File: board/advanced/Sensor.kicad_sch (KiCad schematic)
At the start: 18 parts, among them U6 INA260, U7 BNO086, U8 BME280, Y2 ABS06-32.768KHZ-T

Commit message: put footprints and change schematics
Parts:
- R18: renamed from R20; footprint Resistor_SMD:R_0603_1608Metric -> Resistor_SMD:R_0402_1005Metric
- R19: renamed from R21; footprint Resistor_SMD:R_0603_1608Metric -> Resistor_SMD:R_0402_1005Metric
- R20: renamed from R22; footprint Resistor_SMD:R_0603_1608Metric -> Resistor_SMD:R_0402_1005Metric
- TP1: footprint TestPoint:TestPoint_Loop_D2.50mm_Drill1.85mm -> TestPoint:TestPoint_THTPad_2.0x2.0mm_Drill1.0mm
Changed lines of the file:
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@@
 		(on_board yes)
 		(dnp no)
-		(property "Reference" "#PWR057"
+		(property "Reference" "#PWR059"
 			(at 177.8 100.33 0)
 			(hide yes)
@@
 			(project "TurtlePico-Minimal"
 				(path "/7af2d99d-e350-48e7-86b4-20911ea922f3/399e14dd-2b99-438e-9945-456c74135ff2"
-					(reference "#PWR057")
+					(reference "#PWR059")
 					(unit 1)
 				)
@@
 		(on_board yes)
 		(dnp no)
-		(property "Reference" "#PWR048"
+		(property "Reference" "#PWR050"
 			(at 114.3 93.98 0)
 			(hide yes)
@@
 			(project "TurtlePico-Minimal"
 				(path "/7af2d99d-e350-48e7-86b4-20911ea922f3/399e14dd-2b99-438e-9945-456c74135ff2"
-					(reference "#PWR048")
+					(reference "#PWR050")
 					(unit 1)
 				)
@@
 		(on_board yes)
 		(dnp no)
-		(property "Reference" "#PWR052"
+		(property "Reference" "#PWR054"
 			(at 151.13 119.38 0)
 			(hide yes)
@@
 			(project "TurtlePico-Minimal"
 				(path "/7af2d99d-e350-48e7-86b4-20911ea922f3/399e14dd-2b99-438e-9945-456c74135ff2"
-					(reference "#PWR052")
+					(reference "#PWR054")
 					(unit 1)
 				)
@@
 		(on_board yes)
 		(dnp no)
-		(property "Reference" "#PWR049"
+		(property "Reference" "#PWR051"
 			(at 115.57 52.07 0)
 			(hide yes)
@@
 			(project "TurtlePico-Minimal"
 				(path "/7af2d99d-e350-48e7-86b4-20911ea922f3/399e14dd-2b99-438e-9945-456c74135ff2"
-					(reference "#PWR049")
+					(reference "#PWR051")
 					(unit 1)
 				)
@@
 		(on_board yes)
 		(dnp no)
-		(property "Reference" "#PWR056"
+		(property "Reference" "#PWR058"
 			(at 168.91 143.51 0)
 			(hide yes)
@@
 			(project "TurtlePico-Minimal"
 				(path "/7af2d99d-e350-48e7-86b4-20911ea922f3/399e14dd-2b99-438e-9945-456c74135ff2"
-					(reference "#PWR056")
+					(reference "#PWR058")
 					(unit 1)
 				)
@@
 		(on_board yes)
 		(dnp no)
-		(property "Reference" "#PWR042"
+		(property "Reference" "#PWR044"
 			(at 87.63 119.38 0)
 			(hide yes)
@@
 			(project "TurtlePico-Minimal"
 				(path "/7af2d99d-e350-48e7-86b4-20911ea922f3/399e14dd-2b99-438e-9945-456c74135ff2"
-					(reference "#PWR042")
+					(reference "#PWR044")
 					(unit 1)
 				)
@@
 		(on_board yes)
 		(dnp no)
-		(property "Reference" "#PWR044"
+		(property "Reference" "#PWR046"
 			(at 96.52 77.47 0)
 			(hide yes)
@@
 			(project "TurtlePico-Minimal"
 				(path "/7af2d99d-e350-48e7-86b4-20911ea922f3/399e14dd-2b99-438e-9945-456c74135ff2"
-					(reference "#PWR044")
+					(reference "#PWR046")
 					(unit 1)
 				)
@@
 		(on_board yes)
 		(dnp no)
-		(property "Reference" "#PWR051"
+		(property "Reference" "#PWR053"
 			(at 129.54 133.35 0)
 			(hide yes)
@@
 			(project "TurtlePico-Minimal"
 				(path "/7af2d99d-e350-48e7-86b4-20911ea922f3/399e14dd-2b99-438e-9945-456c74135ff2"
-					(reference "#PWR051")
+					(reference "#PWR053")
 					(unit 1)
 				)
@@
 		(on_board yes)
 		(dnp no)
-		(property "Reference" "#PWR046"
+		(property "Reference" "#PWR048"
 			(at 106.68 113.03 0)
 			(hide yes)
@@
 			(project "TurtlePico-Minimal"
 				(path "/7af2d99d-e350-48e7-86b4-20911ea922f3/399e14dd-2b99-438e-9945-456c74135ff2"
-					(reference "#PWR046")
+					(reference "#PWR048")
 					(unit 1)
 				)
@@
 		(on_board yes)
 		(dnp no)
-		(property "Reference" "R20"
+		(property "Reference" "R18"
 			(at 111.76 50.8 0)
 			(effects
@@
 			)
 		)
-		(property "Footprint" "Resistor_SMD:R_0603_1608Metric"
+		(property "Footprint" "Resistor_SMD:R_0402_1005Metric"
 			(at 109.982 54.61 90)
 			(hide yes)
@@
 			(project "TurtlePico-Minimal"
 				(path "/7af2d99d-e350-48e7-86b4-20911ea922f3/399e14dd-2b99-438e-9945-456c74135ff2"
-					(reference "R20")
+					(reference "R18")
 					(unit 1)
 				)
@@
 		(on_board yes)
 		(dnp no)
-		(property "Reference" "#PWR054"
+		(property "Reference" "#PWR056"
 			(at 166.37 50.8 0)
 			(hide yes)
@@
 			(project "TurtlePico-Minimal"
 				(path "/7af2d99d-e350-48e7-86b4-20911ea922f3/399e14dd-2b99-438e-9945-456c74135ff2"
-					(reference "#PWR054")
+					(reference "#PWR056")
 					(unit 1)
 				)
@@
 		(on_board yes)
 		(dnp no)
-		(property "Reference" "#PWR053"
+		(property "Reference" "#PWR055"
 			(at 151.13 129.54 0)
 			(hide yes)
@@
 			(project "TurtlePico-Minimal"
 				(path "/7af2d99d-e350-48e7-86b4-20911ea922f3/399e14dd-2b99-438e-9945-456c74135ff2"
-					(reference "#PWR053")
+					(reference "#PWR055")
 					(unit 1)
 				)
@@
 			)
 		)
-		(property "Footprint" "TestPoint:TestPoint_Loop_D2.50mm_Drill1.85mm"
+		(property "Footprint" "TestPoint:TestPoint_THTPad_2.0x2.0mm_Drill1.0mm"
 			(at 109.22 53.34 0)
 			(hide yes)
@@
 		(on_board yes)
 		(dnp no)
-		(property "Reference" "R22"
+		(property "Reference" "R20"
 			(at 182.88 109.22 0)
 			(effects
@@
 			)
 		)
-		(property "Footprint" "Resistor_SMD:R_0603_1608Metric"
+		(property "Footprint" "Resistor_SMD:R_0402_1005Metric"
 			(at 186.182 107.95 90)
 			(hide yes)
@@
 			(project "TurtlePico-Minimal"
 				(path "/7af2d99d-e350-48e7-86b4-20911ea922f3/399e14dd-2b99-438e-9945-456c74135ff2"
-					(reference "R22")
+					(reference "R20")
 					(unit 1)
 				)
@@
 		(on_board yes)
 		(dnp no)
-		(property "Reference" "#FLG04"
+		(property "Reference" "#FLG08"
 			(at 96.52 128.905 0)
 			(hide yes)
@@
 			(project "TurtlePico-Minimal"
 				(path "/7af2d99d-e350-48e7-86b4-20911ea922f3/399e14dd-2b99-438e-9945-456c74135ff2"
-					(reference "#FLG04")
+					(reference "#FLG08")
 					(unit 1)
 				)
@@
 		(on_board yes)
 		(dnp no)
-		(property "Reference" "#PWR043"
+		(property "Reference" "#PWR045"
 			(at 96.52 67.31 0)
 			(hide yes)
@@
 			(project "TurtlePico-Minimal"
 				(path "/7af2d99d-e350-48e7-86b4-20911ea922f3/399e14dd-2b99-438e-9945-456c74135ff2"
-					(reference "#PWR043")
+					(reference "#PWR045")
 					(unit 1)
 				)
@@
 		(on_board yes)
 		(dnp no)
-		(property "Reference" "#PWR055"
+		(property "Reference" "#PWR057"
 			(at 168.91 107.95 0)
 			(hide yes)
@@
 			(project "TurtlePico-Minimal"
 				(path "/7af2d99d-e350-48e7-86b4-20911ea922f3/399e14dd-2b99-438e-9945-456c74135ff2"
-					(reference "#PWR055")
+					(reference "#PWR057")
 					(unit 1)
 				)
@@
 		(on_board yes)
 		(dnp no)
-		(property "Reference" "#PWR045"
+		(property "Reference" "#PWR047"
 			(at 96.52 128.27 0)
 			(hide yes)
@@
 			(project "TurtlePico-Minimal"
 				(path "/7af2d99d-e350-48e7-86b4-20911ea922f3/399e14dd-2b99-438e-9945-456c74135ff2"
-					(reference "#PWR045")
+					(reference "#PWR047")
 					(unit 1)
 				)
@@
 		(on_board yes)
 		(dnp no)
-		(property "Reference" "R21"
+		(property "Reference" "R19"
 			(at 113.03 67.31 0)
 			(effects
@@
 			)
 		)
-		(property "Footprint" "Resistor_SMD:R_0603_1608Metric"
+		(property "Footprint" "Resistor_SMD:R_0402_1005Metric"
 			(at 111.252 71.12 90)
 			(hide yes)
@@
 			(project "TurtlePico-Minimal"
 				(path "/7af2d99d-e350-48e7-86b4-20911ea922f3/399e14dd-2b99-438e-9945-456c74135ff2"
-					(reference "R21")
+					(reference "R19")
 					(unit 1)
 				)
@@
 		(on_board yes)
 		(dnp no)
-		(property "Reference" "#PWR047"
+		(property "Reference" "#PWR049"
 			(at 106.68 138.43 0)
 			(hide yes)
@@
 			(project "TurtlePico-Minimal"
 				(path "/7af2d99d-e350-48e7-86b4-20911ea922f3/399e14dd-2b99-438e-9945-456c74135ff2"
-					(reference "#PWR047")
+					(reference "#PWR049")
 					(unit 1)
 				)
@@
 		(on_board yes)
 		(dnp no)
-		(property "Reference" "#PWR050"
+		(property "Reference" "#PWR052"
 			(at 129.54 120.65 0)
 			(hide yes)
@@
 			(project "TurtlePico-Minimal"
 				(path "/7af2d99d-e350-48e7-86b4-20911ea922f3/399e14dd-2b99-438e-9945-456c74135ff2"
-					(reference "#PWR050")
-					(unit 1)
-				)
+					(reference "#PWR052")
+					(unit 1)
+				)

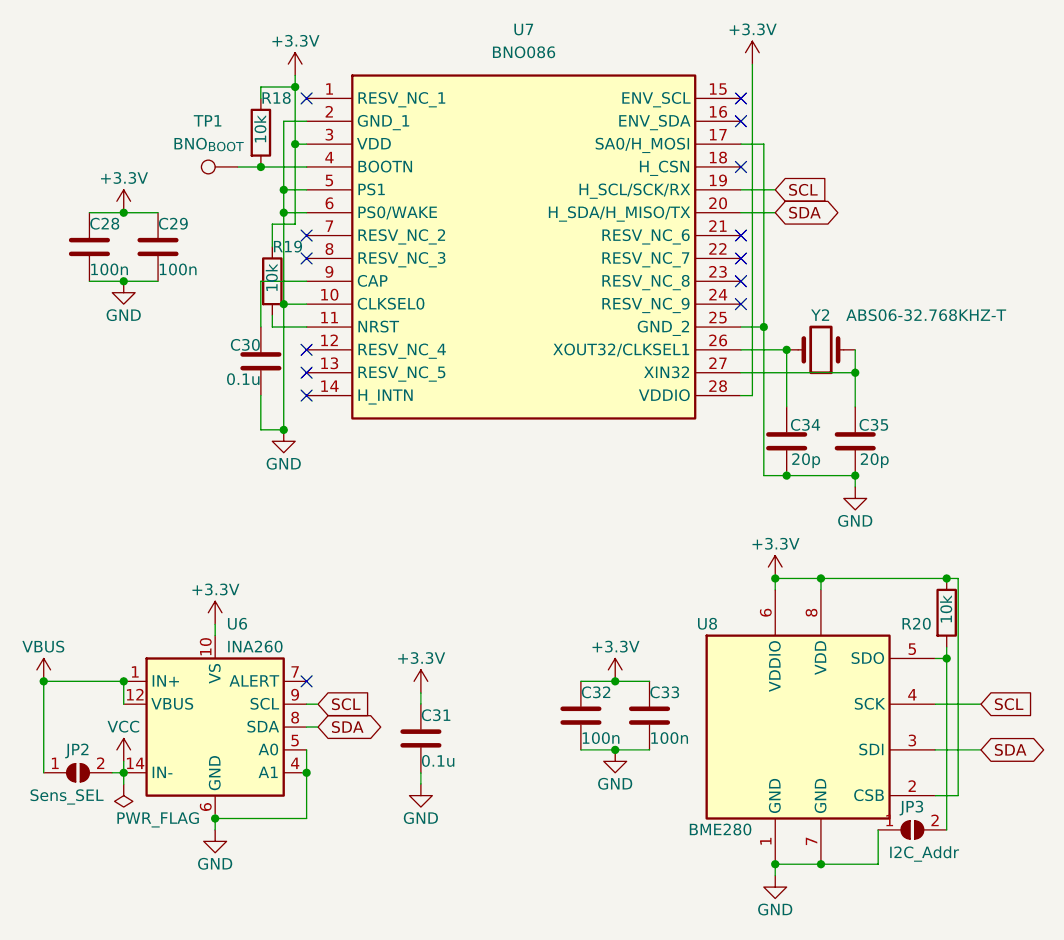
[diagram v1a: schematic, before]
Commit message: change schematics and complete wiring
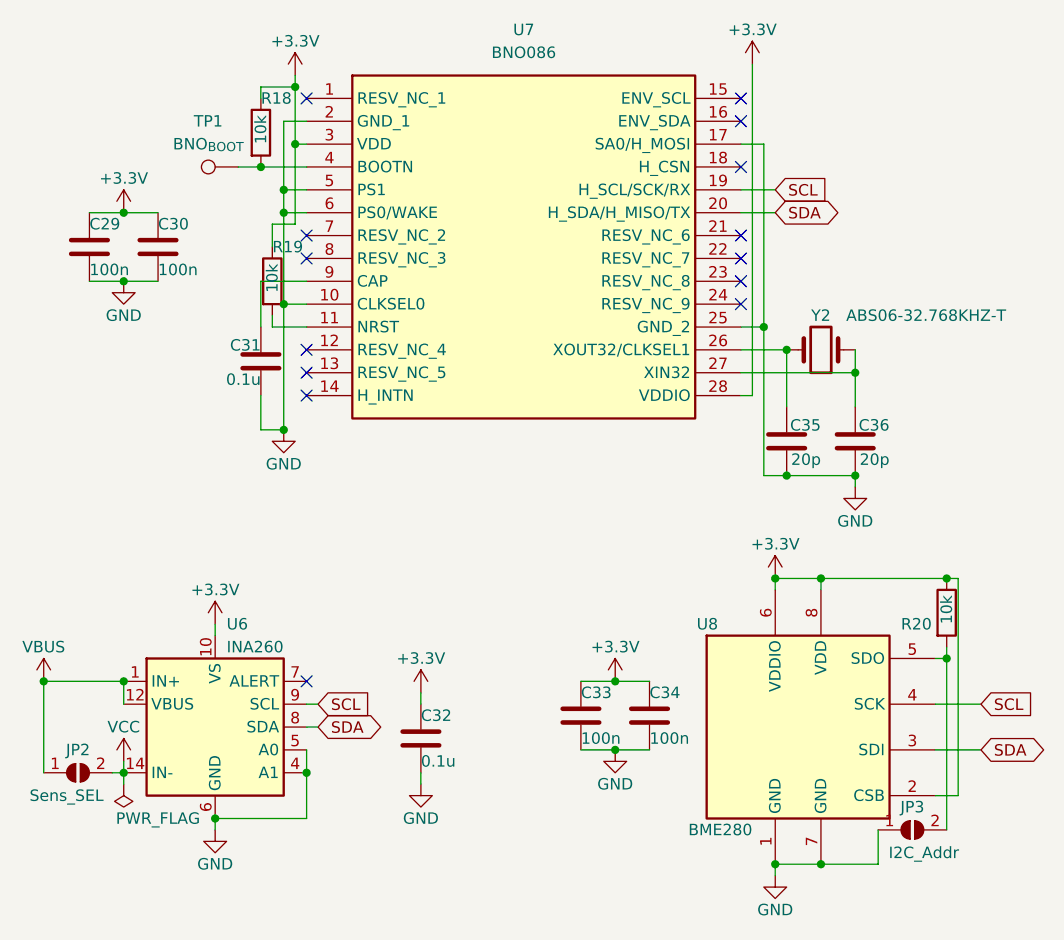
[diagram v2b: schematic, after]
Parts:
- C29: renamed from C28; footprint Capacitor_SMD:C_0201_0603Metric -> C_0402_1005Metric_small_pads:C_0402_1005Metric_small_pads
- C30: renamed from C29; footprint Capacitor_SMD:C_0201_0603Metric -> C_0402_1005Metric_small_pads:C_0402_1005Metric_small_pads
- C31: renamed from C30; footprint Capacitor_SMD:C_0201_0603Metric -> C_0402_1005Metric_small_pads:C_0402_1005Metric_small_pads
- C32: renamed from C31; footprint Capacitor_SMD:C_0201_0603Metric -> C_0402_1005Metric_small_pads:C_0402_1005Metric_small_pads
- C33: renamed from C32; footprint Capacitor_SMD:C_0201_0603Metric -> C_0402_1005Metric_small_pads:C_0402_1005Metric_small_pads
- C34: renamed from C33; footprint Capacitor_SMD:C_0201_0603Metric -> C_0402_1005Metric_small_pads:C_0402_1005Metric_small_pads
- C35: renamed from C34; footprint Capacitor_SMD:C_0201_0603Metric -> C_0402_1005Metric_small_pads:C_0402_1005Metric_small_pads
- C36: renamed from C35; footprint Capacitor_SMD:C_0201_0603Metric -> C_0402_1005Metric_small_pads:C_0402_1005Metric_small_pads
- R18, R19, R20: footprint Resistor_SMD:R_0402_1005Metric -> C_0402_1005Metric_small_pads:C_0402_1005Metric_small_pads

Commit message: add LTB example and more
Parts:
- C29, C30, C31, C32, C33, C34: Mouser Part Number (none) -> 81-GRM15R61A104KA01J; Mouser Price/Stock (none) -> https://www.mouser.jp/ProductDetail/Murata-Electronics/GRM1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
- C35, C36: Mouser Part Number (none) -> 81-GRM1555C1H200JA1D; Mouser Price/Stock (none) -> https://www.mouser.jp/ProductDetail/Murata-Electronics/GRM1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
- R18, R19, R20: Mouser Part Number (none) -> 667-ERJ-2GEJ103X; Mouser Price/Stock (none) -> https://www.mouser.jp/ProductDetail/Panasonic/ERJ-2GEJ103X?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
- U6: Mouser Part Number (none) -> 595-INA260AIPWR; Mouser Price/Stock (none) -> https://www.mouser.jp/ProductDetail/Texas-Instruments/INA26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
- U8: Mouser Part Number (none) -> 262-BME280; Mouser Price/Stock (none) -> https://www.mouser.jp/ProductDetail/Bosch-Sensortec/BME280?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
- Y2: Mouser Part Number (none) -> 815-ABS06-32.768K-T; Mouser Price/Stock (none) -> https://www.mouser.jp/ProductDetail/ABRACON/ABS06-32.768KHZ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
